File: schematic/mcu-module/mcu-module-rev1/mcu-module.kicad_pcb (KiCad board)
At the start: 2 copper layers, 22 parts, among them P1 MCU1, P2 MICROSD-SDIO-CD, P3 SWD, P4 MCU2, U1 STM32F103RE, X1 32768Hz, X2 8MHz

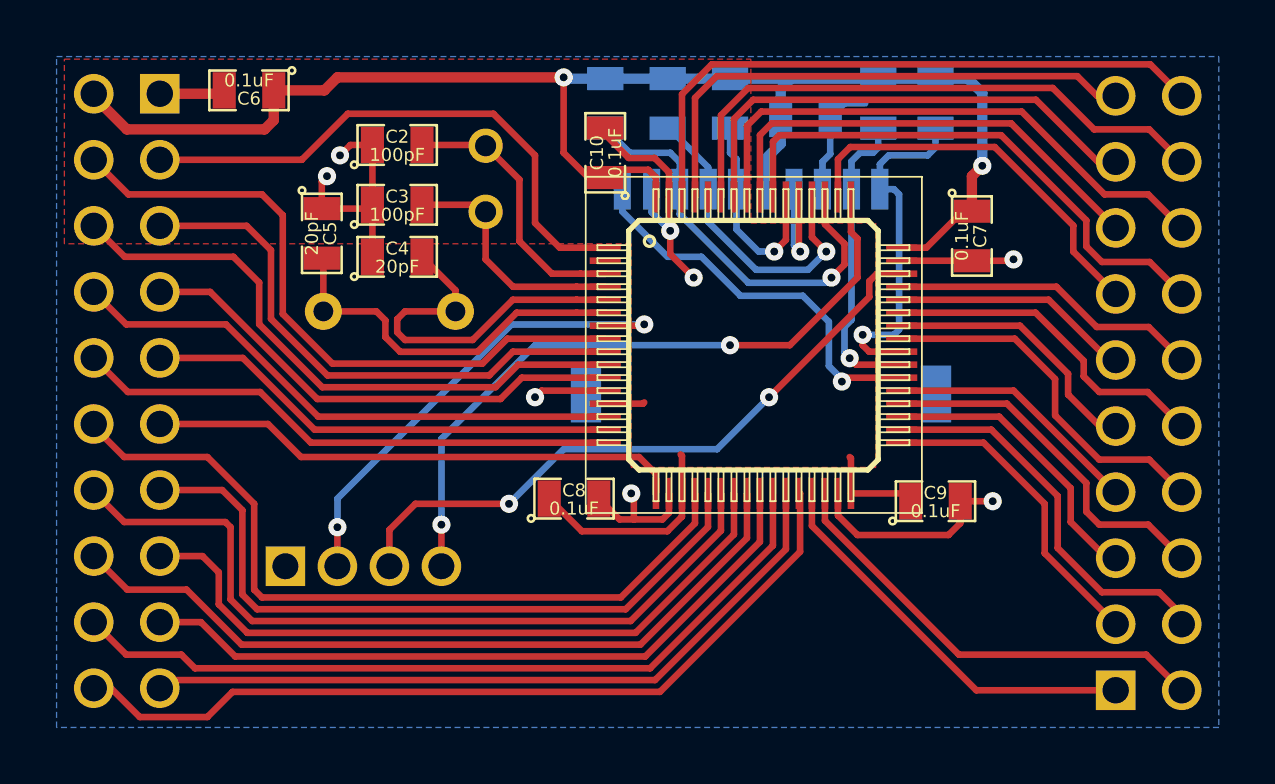
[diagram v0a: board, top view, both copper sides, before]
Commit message: MCU module done
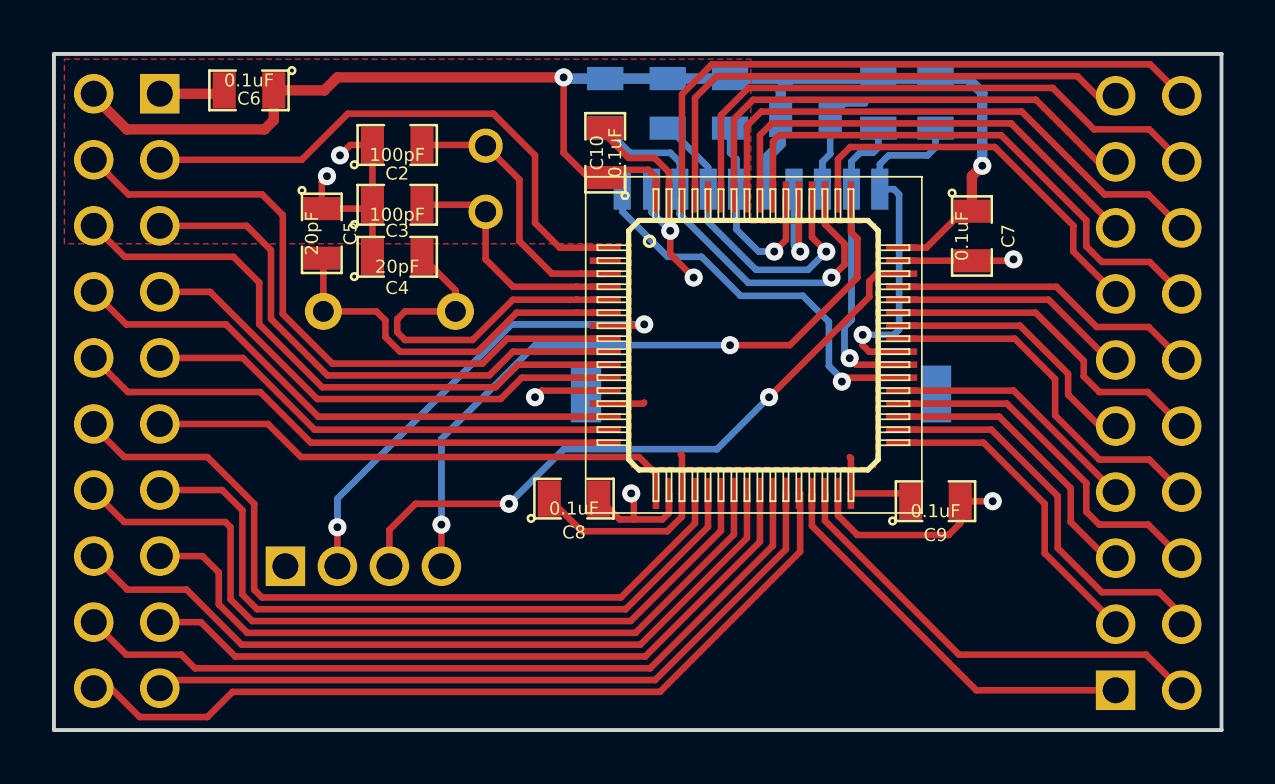
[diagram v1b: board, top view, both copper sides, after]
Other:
- board outline added: 44.9 x 26 mm
